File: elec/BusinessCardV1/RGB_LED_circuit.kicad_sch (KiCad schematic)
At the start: 0 parts

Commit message: Power finished
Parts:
- added C7: 470n, CL10C471JB8NNNC:CAPC1608X90N, symbol CL10C471JB8NNNC:CL10C471JB8NNNC

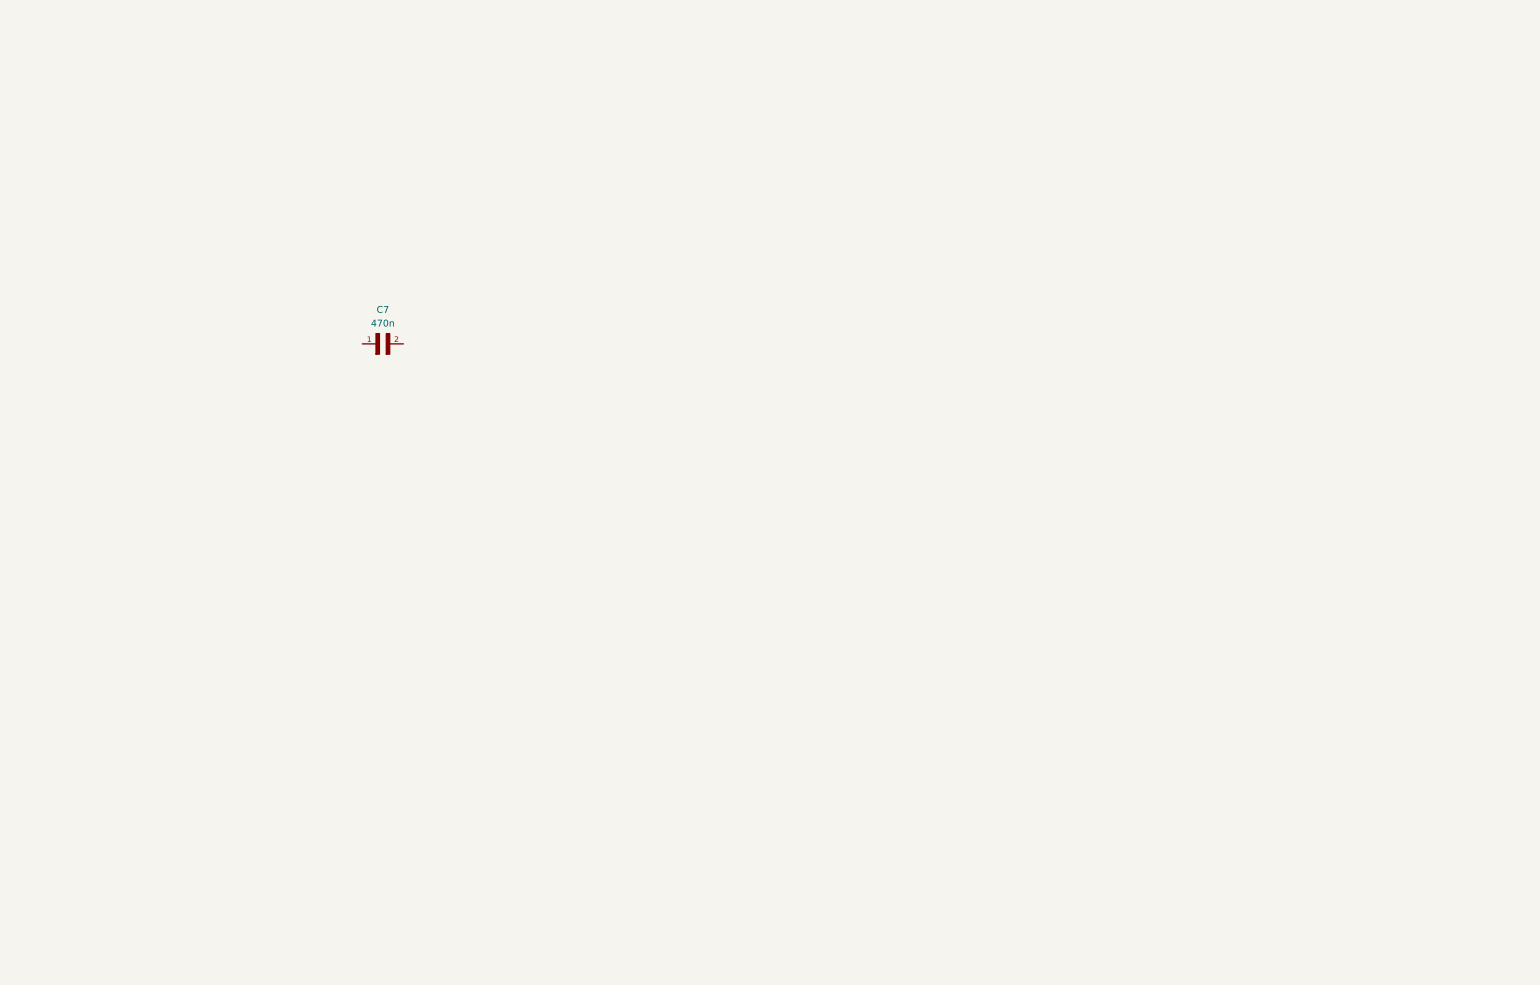
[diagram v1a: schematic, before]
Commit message: Timer and starting LED circuit of RGB
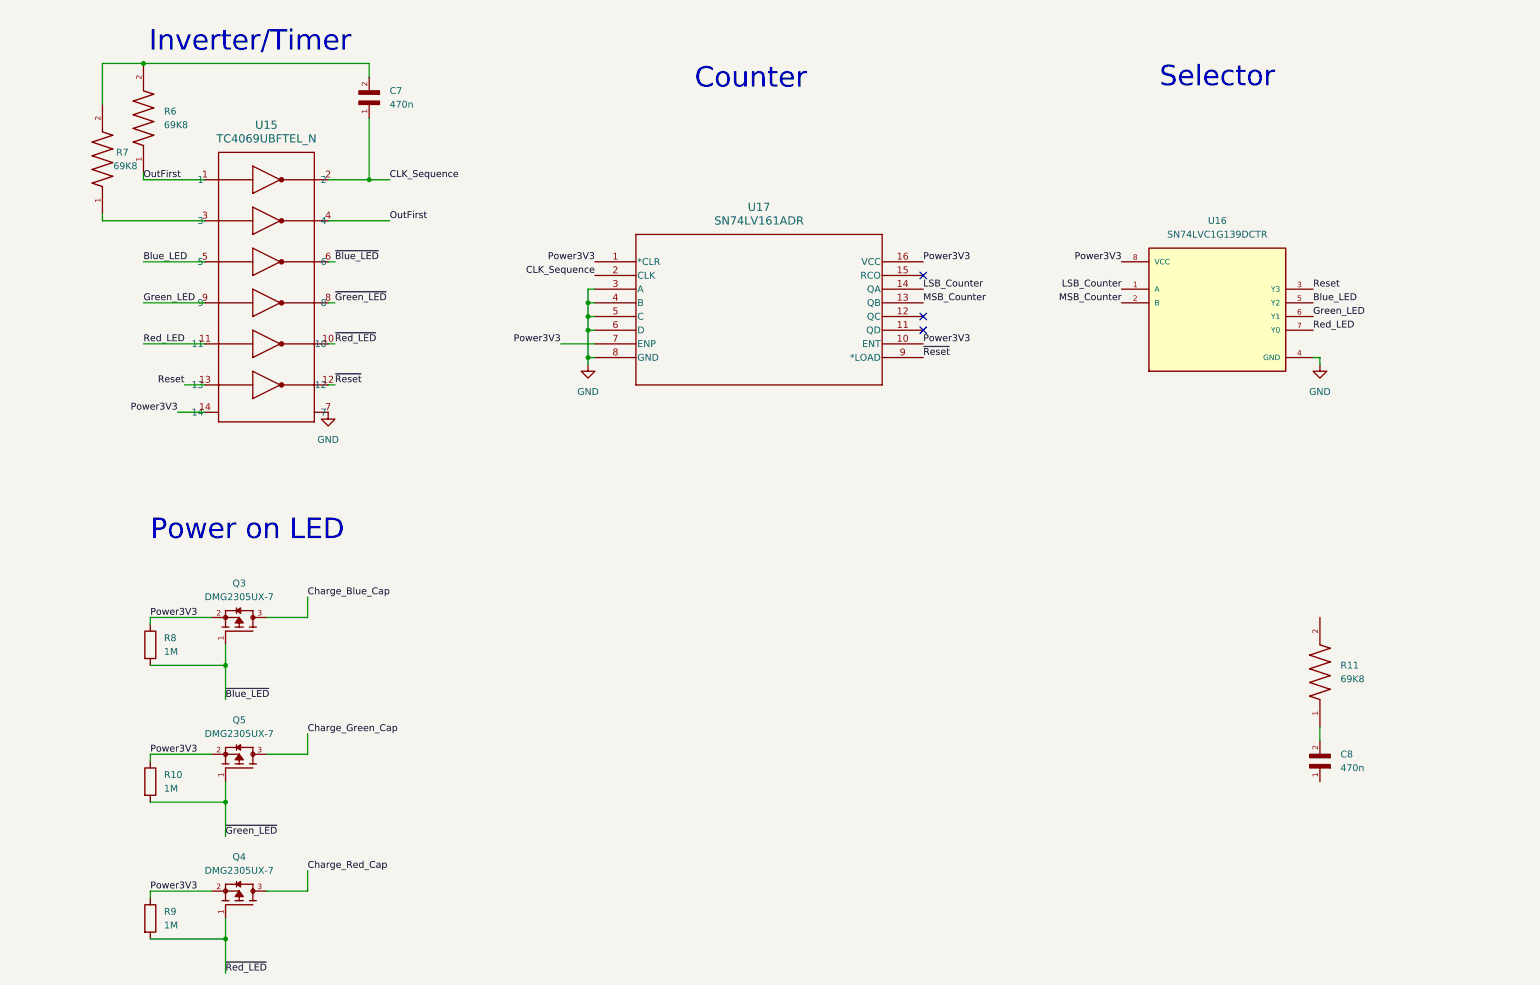
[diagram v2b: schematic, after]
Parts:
- added C8: 470n, CL10C471JB8NNNC:CAPC1608X90N, symbol CL10C471JB8NNNC:CL10C471JB8NNNC
- added Q3, Q4, Q5: DMG2305UX-7, DMG2305UX-7:SOT91P240X110-3N_DMG2305UX-7, symbol DMG2305UX-7:DMG2305UX-7
- added R10, R8, R9: 1M, Resistor_SMD:R_0603_1608Metric_Pad0.98x0.95mm_HandSolder, symbol Device:R
- added R11, R6, R7: 69K8, RC0603FR-0769K8L:RESC1608X55N, symbol RC0603FR-0769K8L:RC0603FR-0769K8L
- added U15: TC4069UBFTEL_N, TSSOP14_TOS, symbol TC4069UBFTELN:TC4069UBFTEL_N
- added U16: SN74LVC1G139DCTR, SN74LVC1G139DCTR:SOP65P400X130-8N, symbol SN74LVC1G139DCTR:SN74LVC1G139DCTR
- added U17: SN74LV161ADR, D16, symbol SN74LV161ADR:SN74LV161ADR
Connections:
- net CLK_Sequence: now reaches C7.1
- net CLK_Sequence: now also U15.2, U17.2 (CLK)
- net at C7.2: now also R6.2, R7.2
- new net: C8.2, R11.1
- new net: R7.1, U15.3
- new net Blue_LED: U15.5, U16.5 (Y2)
- new net Charge_Blue_Cap: Q3.3
- new net Charge_Green_Cap: Q5.3
- new net Charge_Red_Cap: Q4.3
- new net GND: U15.7, U16.4 (GND), U17.3 (A), U17.4 (B), U17.5 (C), U17.6 (D), U17.8 (GND)
- new net Green_LED: U15.9, U16.6 (Y1)
- new net LSB_Counter: U16.1 (A), U17.14 (QA)
- new net MSB_Counter: U16.2 (B), U17.13 (QB)
- new net OutFirst: R6.1, U15.1, U15.4
- new net Power3V3: Q3.2, Q4.2, Q5.2, R10.1, R8.1, R9.1, U15.14, U16.8 (VCC), U17.1 (*CLR), U17.10 (ENT), U17.16 (VCC), U17.7 (ENP)
- new net Red_LED: U15.11, U16.7 (Y0)
- new net Reset: U15.13, U16.3 (Y3)
- new net ~{Blue_LED}: Q3.1, R8.2, U15.6
- new net ~{Green_LED}: Q5.1, R10.2, U15.8
- new net ~{Red_LED}: Q4.1, R9.2, U15.10
- new net ~{Reset}: U15.12, U17.9 (*LOAD)
- no-connect marks 0 -> 3
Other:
- note added: "Counter"
- note added: "Inverter/Timer"
- note added: "Power on LED"
- note added: "Selector"
- moved on the sheet: C7

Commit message: Added timer 555
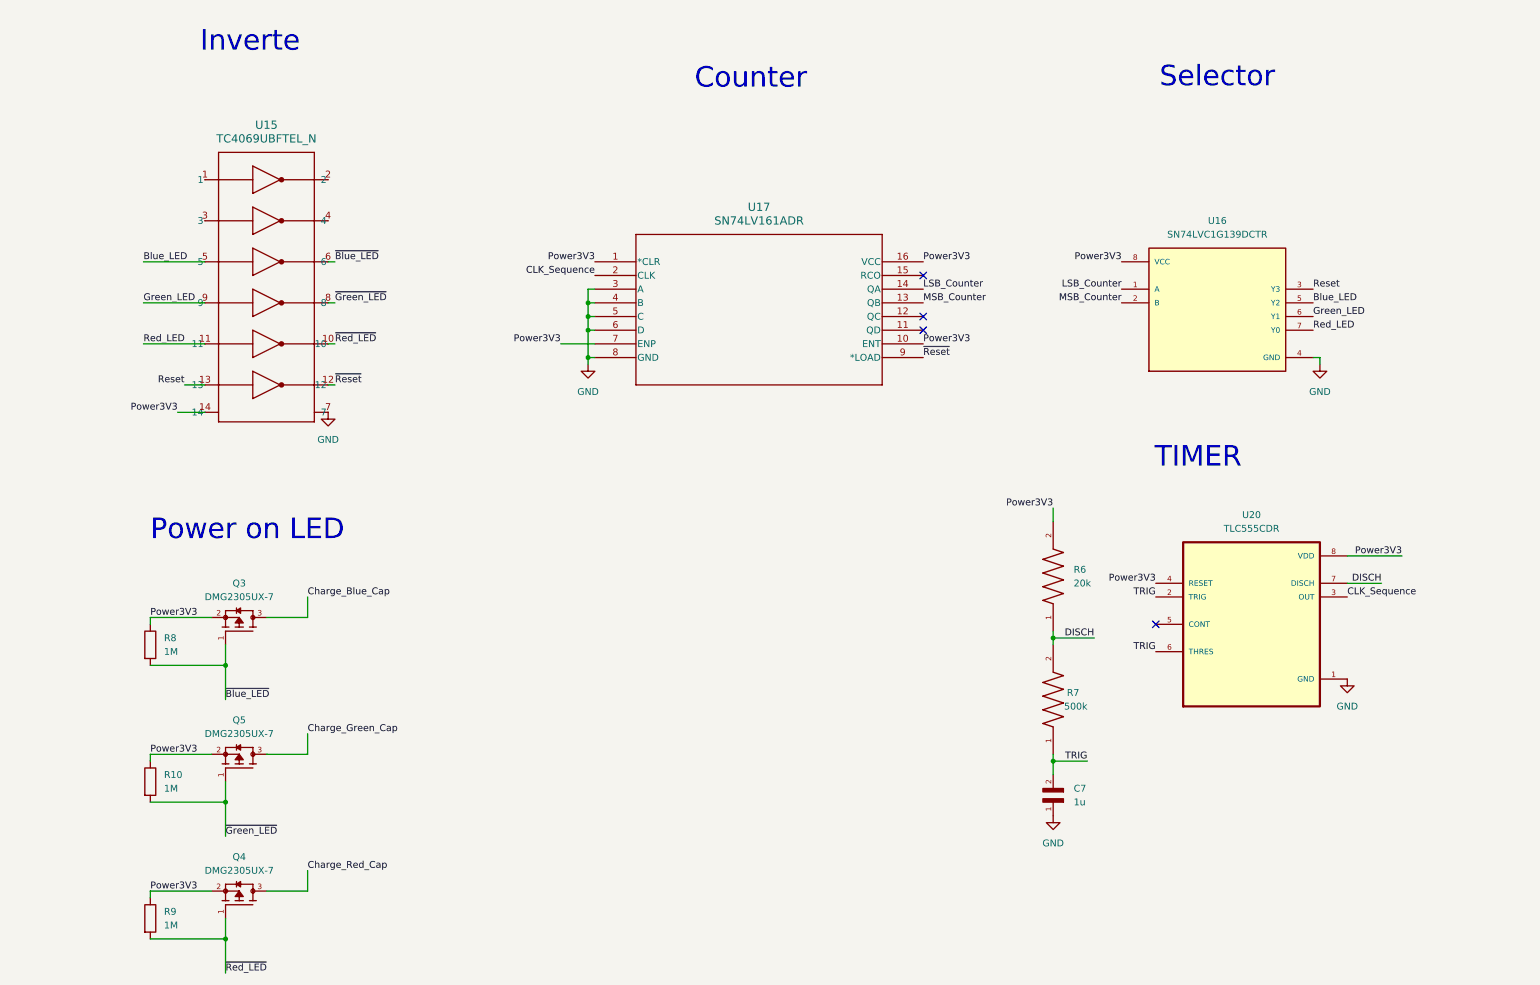
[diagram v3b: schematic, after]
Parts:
- removed C8: 470n, CL10C471JB8NNNC:CAPC1608X90N, symbol CL10C471JB8NNNC:CL10C471JB8NNNC
- removed R11: 69K8, RC0603FR-0769K8L:RESC1608X55N, symbol RC0603FR-0769K8L:RC0603FR-0769K8L
- added U20: TLC555CDR, TLC555CDR:SOIC127P599X175-8N, symbol TLC555CDR:TLC555CDR
- C7: value 470n -> 1u
- R6: value 69K8 -> 20k
- R7: value 69K8 -> 500k
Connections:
- net CLK_Sequence: now also U20.3 (OUT); no longer C7.1, U15.2
- net GND: now also C7.1, U20.1 (GND)
- net Power3V3: now also R6.2, U20.4 (RESET), U20.8 (VDD)
- net at U15.3: no longer R7.1
- removed net OutFirst: R6.1, U15.1, U15.4
- new net DISCH: R6.1, R7.2, U20.7 (DISCH)
- new net TRIG: C7.2, R7.1, U20.2 (TRIG), U20.6 (THRES)
- no-connect marks 3 -> 4
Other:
- note added: "Inverte"
- note added: "TIMER"
- note removed: "Inverter/Timer"
- moved on the sheet: C7, R6, R7

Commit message: Je sais pas trop
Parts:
- R7: value 500k -> 700k
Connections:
- no-connect marks 4 -> 8
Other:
- moved on the sheet: C7, R6, R7, U20

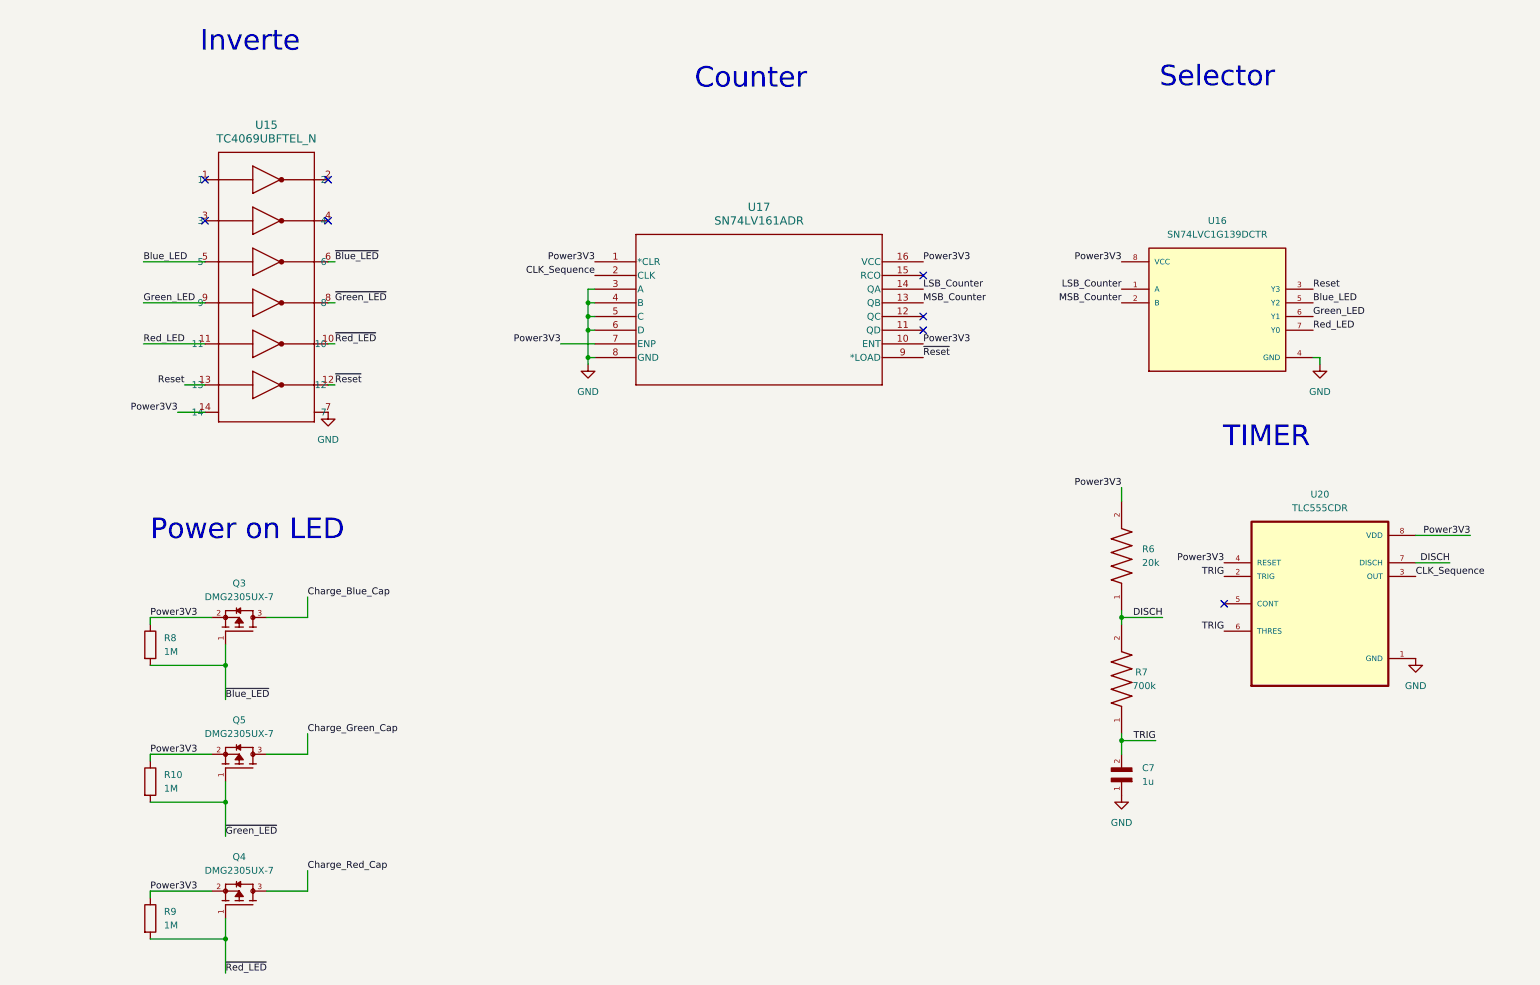
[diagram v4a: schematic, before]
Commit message: Finished LED fade
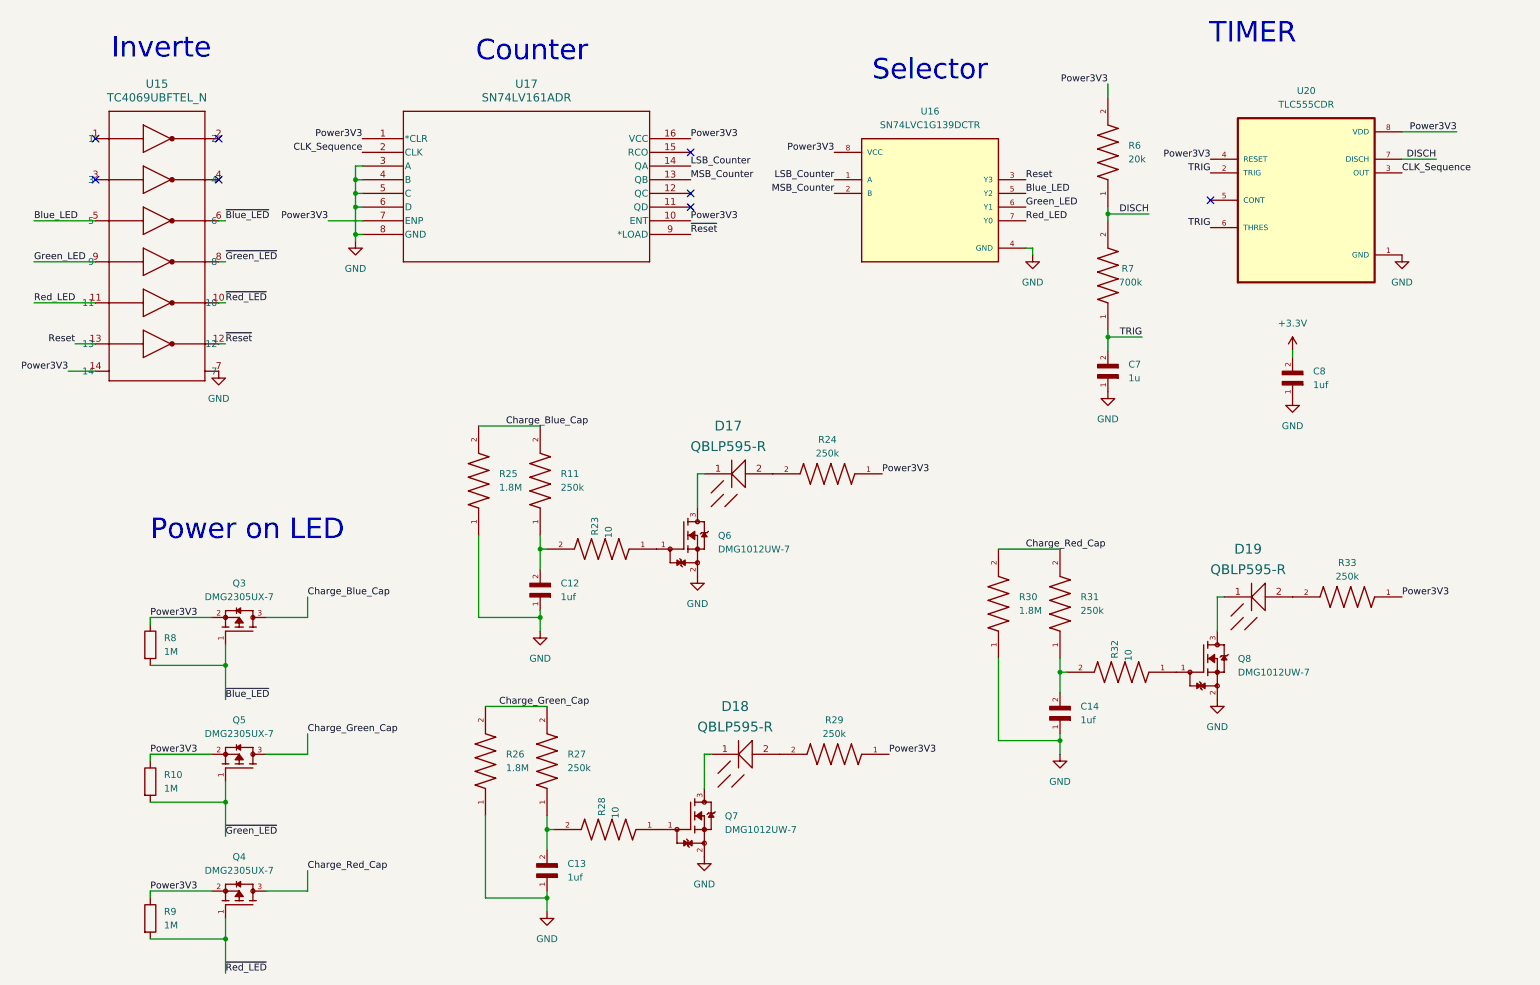
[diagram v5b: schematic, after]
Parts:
- added C12, C13, C14, C8: 1uf, CL10B105KP8NNNC:CAPC1608X90N, symbol CL10B105KP8NNNC:CL10B105KP8NNNC
- added D17, D18, D19: QBLP595-R, FP-QBLP595-R-MFG, symbol QBLP595:QTB-LED-0002
- added Q6, Q7, Q8: DMG1012UW-7, DMG1012UW-7:SOT65P222X110-3N, symbol DMG1012UW-7:DMG1012UW-7
- added R11, R24, R27, R29, R31, R33: 250k, RC0603FR-0769K8L:RESC1608X55N, symbol RC0603FR-0769K8L:RC0603FR-0769K8L
- added R23, R28, R32: 10, RC0603FR-0769K8L:RESC1608X55N, symbol RC0603FR-0769K8L:RC0603FR-0769K8L
- added R25, R26, R30: 1.8M, RC0603FR-0769K8L:RESC1608X55N, symbol RC0603FR-0769K8L:RC0603FR-0769K8L
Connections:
- net Charge_Blue_Cap: now also R11.2, R25.2
- net Charge_Green_Cap: now also R26.2, R27.2
- net Charge_Red_Cap: now also R30.2, R31.2
- net GND: now also C12.1, C13.1, C14.1, C8.1, Q6.2, Q7.2, Q8.2, R25.1, R26.1, R30.1
- net Power3V3: now also R24.1, R29.1, R33.1
- new net: C14.2, R31.1, R32.2
- new net: D17.1 (CATHODE_(-)), Q6.3
- new net: D17.2 (ANODE_(+)), R24.2
- new net: Q7.1, R28.1
- new net: C13.2, R27.1, R28.2
- new net: Q8.1, R32.1
- new net: D19.1 (CATHODE_(-)), Q8.3
- new net: Q6.1, R23.1
- new net: C12.2, R11.1, R23.2
- new net: D19.2 (ANODE_(+)), R33.2
- new net: D18.1 (CATHODE_(-)), Q7.3
- new net: D18.2 (ANODE_(+)), R29.2
- new net +3.3V: C8.2
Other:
- moved on the sheet: C7, R6, R7, U15, U16, U17, U20

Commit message: All footprint and start of PCB
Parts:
- D17, D18, D19: footprint FP-QBLP595-R-MFG -> LED_SMD:LED_0402_1005Metric_Pad0.77x0.64mm_HandSolder
- R24, R29, R33: value 250k -> 180
- U15: footprint TSSOP14_TOS -> TC4069UBFTELN:TSSOP14_TOS
- U17: footprint D16 -> SN74LV161ADR:SN74LV161ADR
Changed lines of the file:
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@@
 			)
 		)
-		(property "Footprint" "FP-QBLP595-R-MFG"
+		(property "Footprint" "LED_SMD:LED_0402_1005Metric_Pad0.77x0.64mm_HandSolder"
 			(at 152.4 96.52 0)
 			(effects
@@
 			)
 		)
-		(property "Footprint" "TSSOP14_TOS"
+		(property "Footprint" "TC4069UBFTELN:TSSOP14_TOS"
 			(at 29.1846 29.21 0)
 			(effects
@@
 			)
 		)
-		(property "Value" "250k"
+		(property "Value" "180"
 			(at 162.56 92.71 0)
 			(effects
@@
 			)
 		)
-		(property "Value" "250k"
+		(property "Value" "180"
 			(at 259.08 115.57 0)
 			(effects
@@
 			)
 		)
-		(property "Footprint" "FP-QBLP595-R-MFG"
+		(property "Footprint" "LED_SMD:LED_0402_1005Metric_Pad0.77x0.64mm_HandSolder"
 			(at 153.67 148.59 0)
 			(effects
@@
 			)
 		)
-		(property "Footprint" "D16"
+		(property "Footprint" "SN74LV161ADR:SN74LV161ADR"
 			(at 76.2 34.29 0)
 			(effects
@@
 			)
 		)
-		(property "Value" "250k"
+		(property "Value" "180"
 			(at 163.83 144.78 0)
 			(effects
@@
 			)
 		)
-		(property "Footprint" "FP-QBLP595-R-MFG"
+		(property "Footprint" "LED_SMD:LED_0402_1005Metric_Pad0.77x0.64mm_HandSolder"
 			(at 248.92 119.38 0)
 			(effects
